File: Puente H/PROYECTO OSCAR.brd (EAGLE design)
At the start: 38 x 35.4 mm, 8 parts, among them IC1 L293D

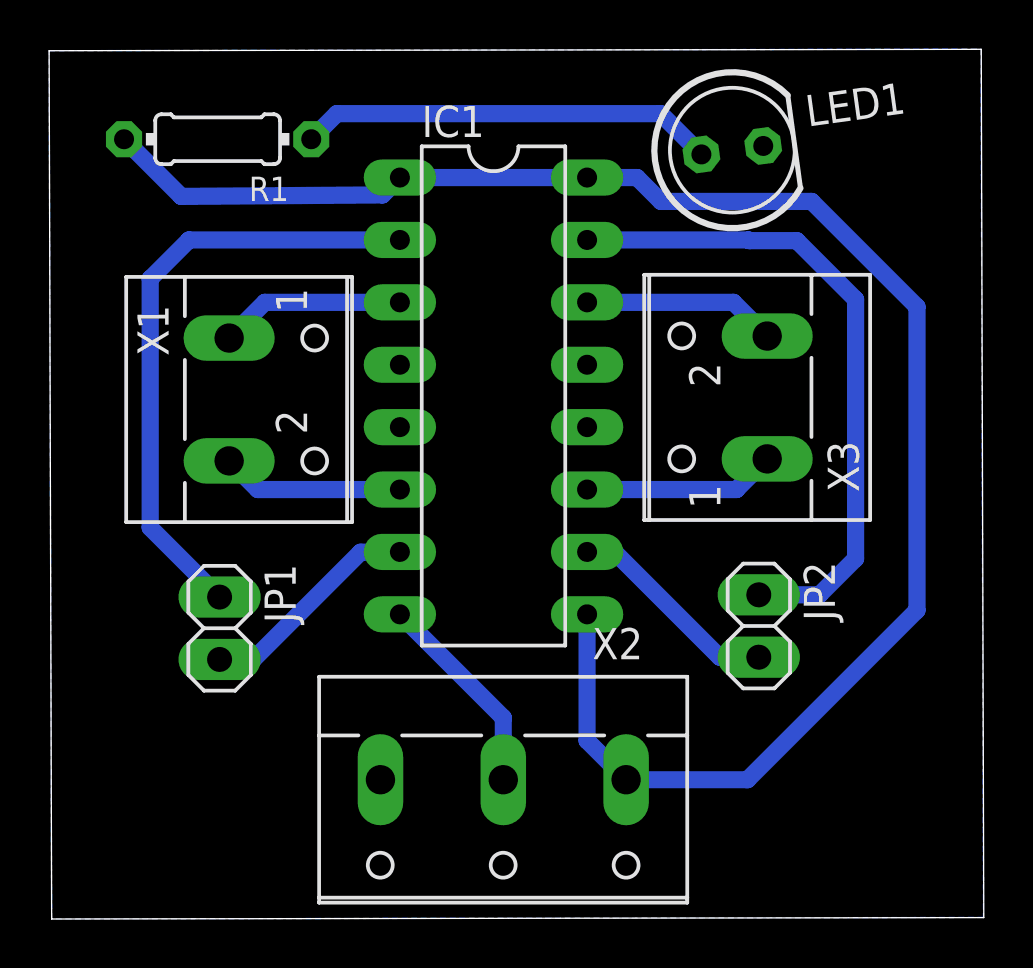
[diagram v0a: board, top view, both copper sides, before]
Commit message: Se añade el puente H, y los gerber para las PCBs anteriores
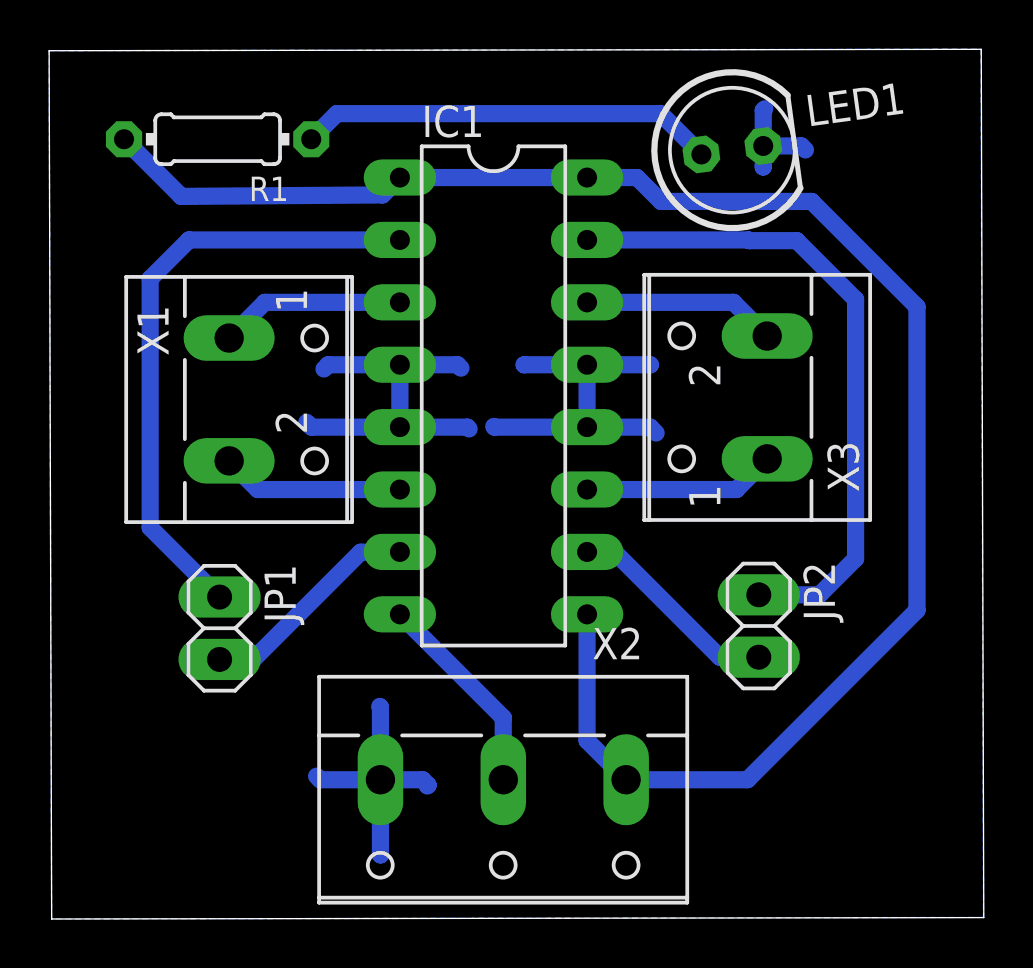
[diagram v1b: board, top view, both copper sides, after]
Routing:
- net GND: track 0.00 -> 44.4 mm
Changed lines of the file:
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@@
 <vertex x="37.932284375" y="0.064565625"/>
 </polygon>
+<wire x1="13.38380625" y1="5.669696875" x2="15.10186875" y2="5.669696875" width="0.7" layer="16"/>
+<wire x1="15.10186875" y1="5.669696875" x2="15.324621875" y2="5.44694375" width="0.7" layer="16"/>
+<wire x1="15.324621875" y1="5.44694375" x2="15.29125" y2="5.413571875" width="0.7" layer="16"/>
+<wire x1="13.38380625" y1="5.669696875" x2="13.38380625" y2="8.62594375" width="0.7" layer="16"/>
+<wire x1="13.38380625" y1="8.62594375" x2="13.354790625" y2="8.654959375" width="0.7" layer="16"/>
+<wire x1="13.38380625" y1="5.669696875" x2="13.38380625" y2="2.610884375" width="0.7" layer="16"/>
+<wire x1="13.38380625" y1="2.610884375" x2="13.388178125" y2="2.6065125" width="0.7" layer="16"/>
+<wire x1="13.38380625" y1="5.669696875" x2="10.928825" y2="5.669696875" width="0.7" layer="16"/>
+<wire x1="10.928825" y1="5.669696875" x2="10.78399375" y2="5.814528125" width="0.7" layer="16"/>
+<wire x1="14.1754125" y1="20.021603125" x2="16.922215625" y2="20.021603125" width="0.7" layer="16"/>
+<wire x1="16.922215625" y1="20.021603125" x2="16.993971875" y2="19.949846875" width="0.7" layer="16"/>
+<wire x1="14.1754125" y1="22.561603125" x2="16.521190625" y2="22.561603125" width="0.7" layer="16"/>
+<wire x1="16.521190625" y1="22.561603125" x2="16.6601" y2="22.42269375" width="0.7" layer="16"/>
+<wire x1="14.1754125" y1="22.561603125" x2="14.1754125" y2="20.021603125" width="0.7" layer="16"/>
+<wire x1="21.7954125" y1="22.561603125" x2="21.7954125" y2="20.021603125" width="0.7" layer="16"/>
+<wire x1="21.7954125" y1="22.561603125" x2="19.23614375" y2="22.561603125" width="0.7" layer="16"/>
+<wire x1="19.23614375" y1="22.561603125" x2="19.2309" y2="22.556359375" width="0.7" layer="16"/>
+<wire x1="21.7954125" y1="22.561603125" x2="24.36725" y2="22.561603125" width="0.7" layer="16"/>
+<wire x1="24.36725" y1="22.561603125" x2="24.37249375" y2="22.556359375" width="0.7" layer="16"/>
+<wire x1="21.7954125" y1="20.021603125" x2="24.3673625" y2="20.021603125" width="0.7" layer="16"/>
+<wire x1="24.3673625" y1="20.021603125" x2="24.606203125" y2="19.7827625" width="0.7" layer="16"/>
+<wire x1="21.7954125" y1="20.021603125" x2="18.024075" y2="20.021603125" width="0.7" layer="16"/>
+<wire x1="18.024075" y1="20.021603125" x2="17.99558125" y2="20.050096875" width="0.7" layer="16"/>
+<wire x1="14.1754125" y1="20.021603125" x2="10.578928125" y2="20.021603125" width="0.7" layer="16"/>
+<wire x1="10.578928125" y1="20.021603125" x2="10.38335" y2="20.21718125" width="0.7" layer="16"/>
+<wire x1="14.1754125" y1="22.561603125" x2="11.256803125" y2="22.561603125" width="0.7" layer="16"/>
+<wire x1="11.256803125" y1="22.561603125" x2="11.084475" y2="22.389275" width="0.7" layer="16"/>
+<wire x1="28.9652125" y1="31.467765625" x2="30.52071875" y2="31.467765625" width="0.7" layer="16"/>
+<wire x1="30.52071875" y1="31.467765625" x2="30.684146875" y2="31.3043375" width="0.7" layer="16"/>
+<wire x1="28.9652125" y1="31.467765625" x2="28.9652125" y2="32.915596875" width="0.7" layer="16"/>
+<wire x1="28.9652125" y1="32.915596875" x2="29.030375" y2="32.980759375" width="0.7" layer="16"/>
+<wire x1="28.9652125" y1="31.467765625" x2="28.9652125" y2="30.61166875" width="0.7" layer="16"/>
+<wire x1="28.9652125" y1="30.61166875" x2="28.96333125" y2="30.6097875" width="0.7" layer="16"/>
 </signal>
 <signal name="N$2">
